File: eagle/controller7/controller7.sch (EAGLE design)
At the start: 86 parts, among them IC1 ILD213T, IC2 ILD213T, Q1 2.5A/30V, Q2 200mA/50V, U2 MP2307, U3 MP2307, X1 1501_04, X2 ZX62D-B-5PA8

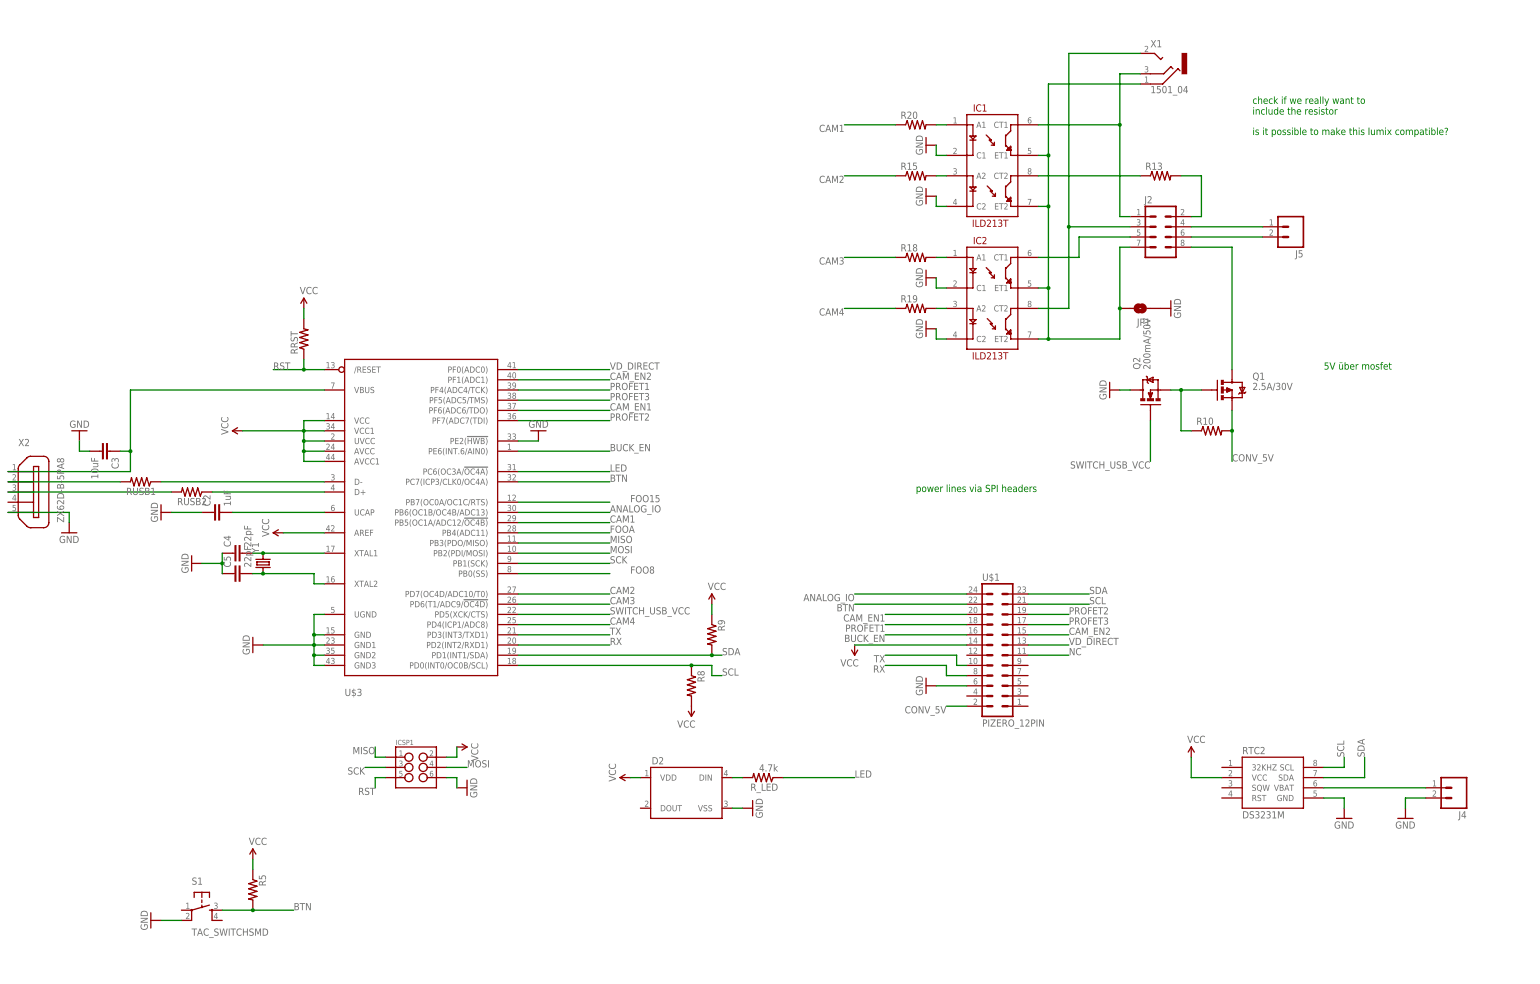
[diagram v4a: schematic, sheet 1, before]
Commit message: controller7: controllerboard nearly finished
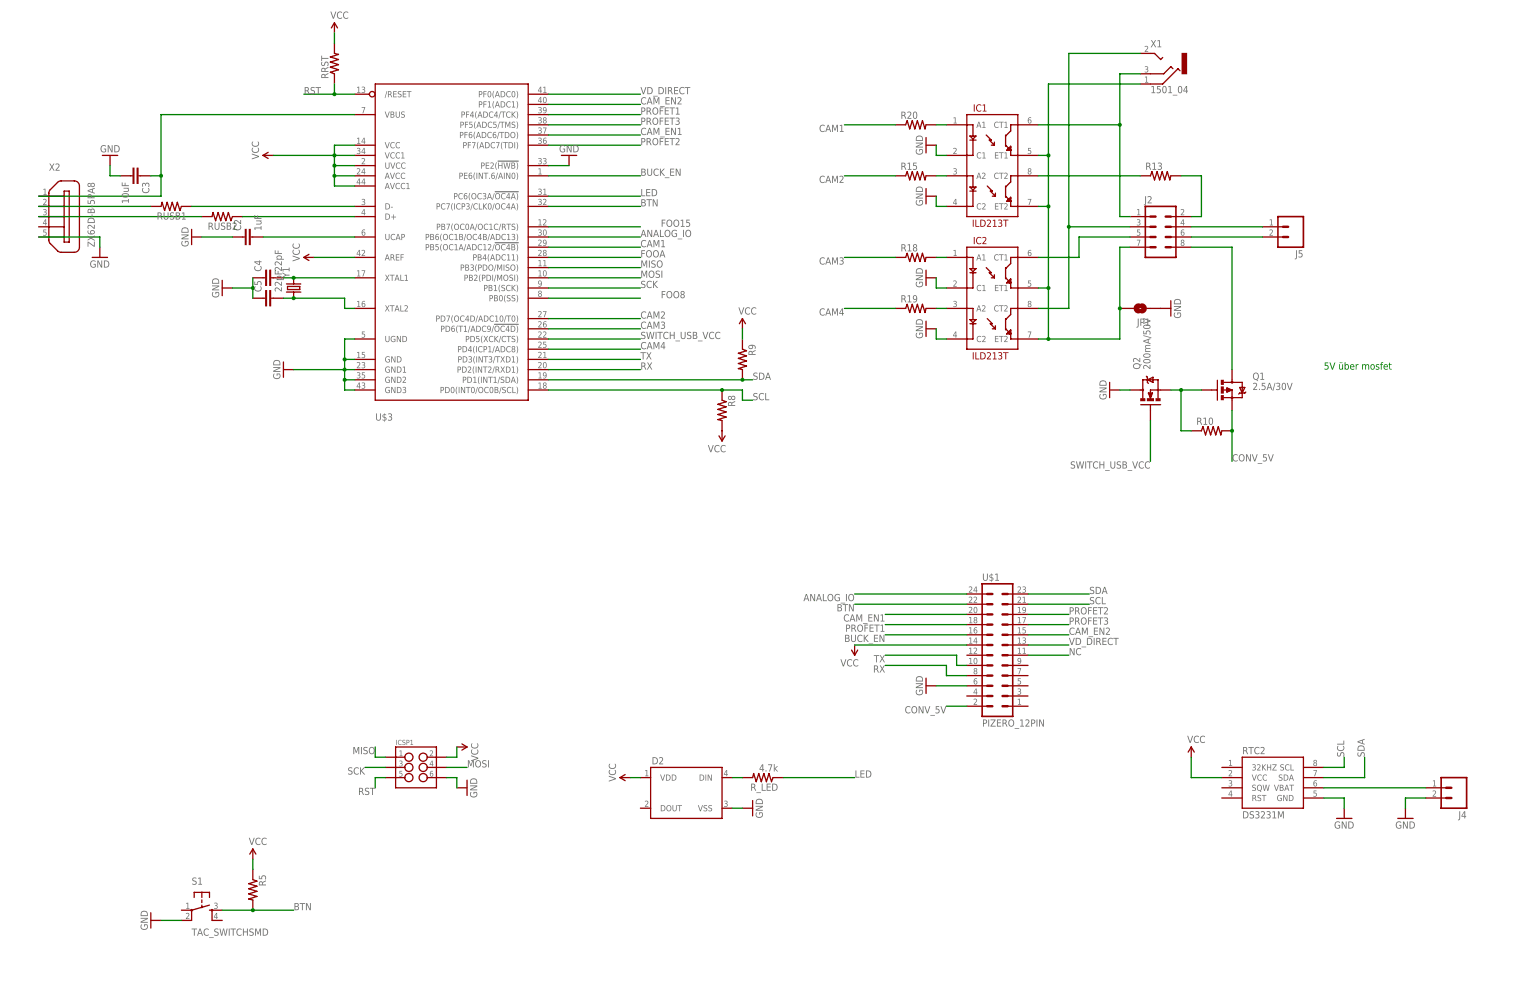
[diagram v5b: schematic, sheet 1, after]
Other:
- note removed: "check if we really want to include the resistor"
- note removed: "is it possible to make this lumix compatible?"
- note removed: "power lines via SPI headers"
- moved on the sheet: C2, C3, C4, C5, R8, R9, RRST, RUSB1, RUSB2, U$3, X2, Y1

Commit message: controller7: controllerboard finished
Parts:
- added C1: 0.1uF (low leakage), SparkFun-Capacitors:CAP1206
- added F2: PTCSMD-W, SparkFun-PowerIC:PTCSMD-W
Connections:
- removed net FOO15: U$3.PB7(OC0A/OC1C/RTS)
- removed net FOO8: U$3.PB0(SS)
- removed net VBAT1: J4.1, RTC2.VBAT
- new net N$38: F2.1, X2G$1.1
- new net N$39: C1.1, J4.1, RTC2.VBAT
- net GND: now also C1.2
- net N$22: now also F2.2; no longer X2G$1.1
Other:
- moved on the sheet: C3

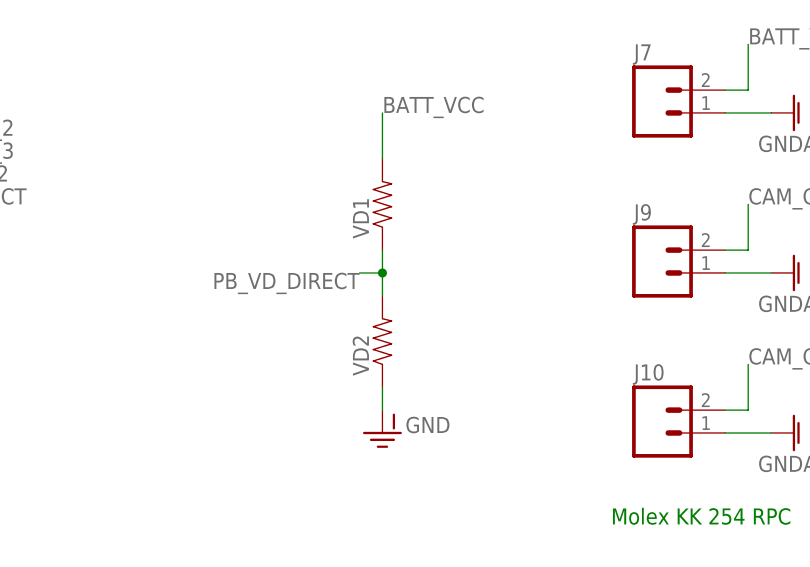
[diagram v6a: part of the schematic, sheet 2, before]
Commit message: controller7: values for voltage divider resistors
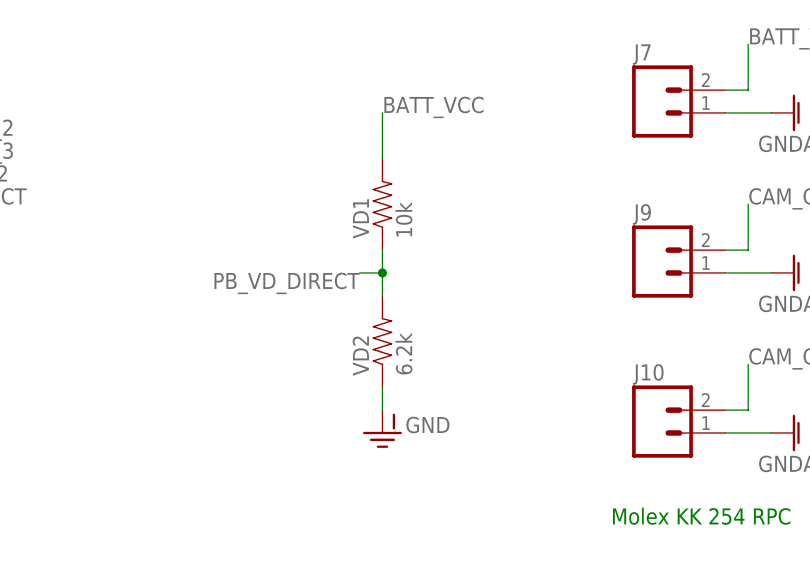
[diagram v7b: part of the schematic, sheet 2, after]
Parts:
- VD1: value (none) -> 10k
- VD2: value (none) -> 6.2k
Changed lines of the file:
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@@
 <?xml version="1.0" encoding="utf-8"?>
 <!DOCTYPE eagle SYSTEM "eagle.dtd">
-<eagle version="7.7.0">
+<eagle version="8.0.1">
 <drawing>
 <settings>
@@
 <grid distance="0.1" unitdist="inch" unit="inch" style="lines" multiple="1" display="no" altdistance="0.01" altunitdist="inch" altunit="inch"/>
 <layers>
-<layer number="1" name="Top" color="4" fill="1" visible="yes" active="no"/>
-<layer number="16" name="Bottom" color="1" fill="1" visible="yes" active="no"/>
-<layer number="17" name="Pads" color="2" fill="1" visible="yes" active="no"/>
-<layer number="18" name="Vias" color="2" fill="1" visible="yes" active="no"/>
-<layer number="19" name="Unrouted" color="6" fill="1" visible="yes" active="no"/>
-<layer number="20" name="Dimension" color="15" fill="1" visible="yes" active="no"/>
-<layer number="21" name="tPlace" color="7" fill="1" visible="yes" active="no"/>
-<layer number="22" name="bPlace" color="7" fill="1" visible="yes" active="no"/>
-<layer number="23" name="tOrigins" color="15" fill="1" visible="yes" active="no"/>
-<layer number="24" name="bOrigins" color="15" fill="1" visible="yes" active="no"/>
-<layer number="25" name="tNames" color="7" fill="1" visible="yes" active="no"/>
-<layer number="26" name="bNames" color="7" fill="1" visible="yes" active="no"/>
-<layer number="27" name="tValues" color="7" fill="1" visible="yes" active="no"/>
-<layer number="28" name="bValues" color="7" fill="1" visible="yes" active="no"/>
+<layer number="1" name="Top" color="4" fill="1" visible="no" active="no"/>
+<layer number="16" name="Bottom" color="1" fill="1" visible="no" active="no"/>
+<layer number="17" name="Pads" color="2" fill="1" visible="no" active="no"/>
+<layer number="18" name="Vias" color="2" fill="1" visible="no" active="no"/>
+<layer number="19" name="Unrouted" color="6" fill="1" visible="no" active="no"/>
+<layer number="20" name="Dimension" color="15" fill="1" visible="no" active="no"/>
+<layer number="21" name="tPlace" color="7" fill="1" visible="no" active="no"/>
+<layer number="22" name="bPlace" color="7" fill="1" visible="no" active="no"/>
+<layer number="23" name="tOrigins" color="15" fill="1" visible="no" active="no"/>
+<layer number="24" name="bOrigins" color="15" fill="1" visible="no" active="no"/>
+<layer number="25" name="tNames" color="7" fill="1" visible="no" active="no"/>
+<layer number="26" name="bNames" color="7" fill="1" visible="no" active="no"/>
+<layer number="27" name="tValues" color="7" fill="1" visible="no" active="no"/>
+<layer number="28" name="bValues" color="7" fill="1" visible="no" active="no"/>
 <layer number="29" name="tStop" color="7" fill="3" visible="no" active="no"/>
 <layer number="30" name="bStop" color="7" fill="6" visible="no" active="no"/>
@@
 <layer number="35" name="tGlue" color="7" fill="4" visible="no" active="no"/>
 <layer number="36" name="bGlue" color="7" fill="5" visible="no" active="no"/>
-<layer number="37" name="tTest" color="7" fill="1" visible="yes" active="no"/>
-<layer number="38" name="bTest" color="7" fill="1" visible="yes" active="no"/>
+<layer number="37" name="tTest" color="7" fill="1" visible="no" active="no"/>
+<layer number="38" name="bTest" color="7" fill="1" visible="no" active="no"/>
 <layer number="39" name="tKeepout" color="4" fill="11" visible="no" active="no"/>
 <layer number="40" name="bKeepout" color="1" fill="11" visible="no" active="no"/>
@@
 <layer number="44" name="Drills" color="7" fill="1" visible="no" active="no"/>
 <layer number="45" name="Holes" color="7" fill="1" visible="no" active="no"/>
-<layer number="46" name="Milling" color="3" fill="1" visible="yes" active="no"/>
-<layer number="47" name="Measures" color="7" fill="1" visible="yes" active="no"/>
-<layer number="48" name="Document" color="7" fill="1" visible="yes" active="no"/>
-<layer number="49" name="Reference" color="7" fill="1" visible="yes" active="no"/>
-<layer number="50" name="dxf" color="7" fill="1" visible="yes" active="no"/>
-<layer number="51" name="tDocu" color="7" fill="1" visible="yes" active="no"/>
-<layer number="52" name="bDocu" color="7" fill="1" visible="yes" active="no"/>
-<layer number="53" name="tGND_GNDA" color="7" fill="9" visible="yes" active="no"/>
-<layer number="54" name="bGND_GNDA" color="1" fill="9" visible="yes" active="no"/>
-<layer number="56" name="wert" color="7" fill="1" visible="yes" active="no"/>
-<layer number="57" name="tCAD" color="7" fill="1" visible="yes" active="no"/>
-<layer number="59" name="tCarbon" color="7" fill="1" visible="yes" active="no"/>
-<layer number="60" name="bCarbon" color="7" fill="1" visible="yes" active="no"/>
+<layer number="46" name="Milling" color="3" fill="1" visible="no" active="no"/>
+<layer number="47" name="Measures" color="7" fill="1" visible="no" active="no"/>
+<layer number="48" name="Document" color="7" fill="1" visible="no" active="no"/>
+<layer number="49" name="Reference" color="7" fill="1" visible="no" active="no"/>
+<layer number="50" name="dxf" color="7" fill="1" visible="no" active="no"/>
+<layer number="51" name="tDocu" color="7" fill="1" visible="no" active="no"/>
+<layer number="52" name="bDocu" color="7" fill="1" visible="no" active="no"/>
+<layer number="53" name="tGND_GNDA" color="7" fill="9" visible="no" active="no"/>
+<layer number="54" name="bGND_GNDA" color="1" fill="9" visible="no" active="no"/>
+<layer number="56" name="wert" color="7" fill="1" visible="no" active="no"/>
+<layer number="57" name="tCAD" color="7" fill="1" visible="no" active="no"/>
+<layer number="59" name="tCarbon" color="7" fill="1" visible="no" active="no"/>
+<layer number="60" name="bCarbon" color="7" fill="1" visible="no" active="no"/>
 <layer number="90" name="Modules" color="5" fill="1" visible="yes" active="yes"/>
 <layer number="91" name="Nets" color="2" fill="1" visible="yes" active="yes"/>
@@
 <part name="R8" library="SparkFun-Passives" deviceset="RESISTOR" device="1206"/>
 <part name="R9" library="SparkFun-Passives" deviceset="RESISTOR" device="1206"/>
-<part name="VD1" library="SparkFun-Passives" deviceset="RESISTOR" device="1206"/>
-<part name="VD2" library="SparkFun-Passives" deviceset="RESISTOR" device="1206"/>
+<part name="VD1" library="SparkFun-Passives" deviceset="RESISTOR" device="1206" value="10k"/>
+<part name="VD2" library="SparkFun-Passives" deviceset="RESISTOR" device="1206" value="6.2k"/>
 <part name="C2" library="SparkFun-Capacitors" deviceset="CAP" device="1206" value="1uF"/>
 <part name="GND14" library="SparkFun-Aesthetics" deviceset="GND" device=""/>
